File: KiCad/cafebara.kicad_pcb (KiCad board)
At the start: 4 copper layers, 49 x 32 mm, 54 parts, among them J1 Micro_SD_Card_Det2, J2 USB_C_Receptacle_USB2.0_14P, J3 PROG, J4 Conn_01x19_MountingPin, J5 I2C, J6 EDID, Q1 NMOS, SW1 SW_Push, U3 ATtiny1616-M, U4 M24C02-WMN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

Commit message: Various improvements and misc changes
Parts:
- added C17: 22uF, Capacitor_SMD:C_0402_1005Metric, F.Cu at (102.5, 68.0)
- added C18: 22uF, Capacitor_SMD:C_0402_1005Metric, F.Cu at (102.5, 67.0)
- added R9: 1k, Resistor_SMD:R_0402_1005Metric, F.Cu at (70.5, 52.0)
- C10, C11: value 10uF -> 22uF; footprint Capacitor_SMD:C_0402_1005Metric -> Capacitor_SMD:C_0805_2012Metric
- C7, J6: moved to F.Cu
- U4: value M24C02-WMN -> M24C02-RMC; footprint Package_SO:SOIC-8_3.9x4.9mm_P1.27mm -> cafebara:UFDFPN_RMC; moved to F.Cu
- moved TP3 17.5 mm to (113.8, 49.0)
- moved C7 17.0 mm to (70.0, 49.2), turned to 90 degrees
- moved TP2 15.5 mm to (90.5, 72.2), turned to 180 degrees
- moved J6 14.9 mm to (68.0, 52.5), turned to 0 degrees
- moved U4 13.9 mm to (67.8, 49.0)
- moved TP1 13.7 mm to (92.5, 72.2), turned to 180 degrees
- moved R4 13.6 mm to (111.5, 50.2), turned to -90 degrees
- moved TP10 13.2 mm to (113.8, 47.2), turned to 180 degrees
- moved TP6 11.2 mm to (87.5, 72.0), turned to 180 degrees
- moved C13 4.32 mm to (108.5, 71.5), turned to -45 degrees
- moved C15 3.18 mm to (94.8, 65.8), turned to 90 degrees
- moved J3 2.55 mm to (114.0, 51.8)
- moved C4 2.02 mm to (90.2, 58.8), turned to 180 degrees
- moved C11 1.90 mm to (106.5, 65.8)
- moved C9 1.75 mm to (92.8, 68.0)
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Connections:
- U3 pad 18: unconnected-(U3-PC3-Pad18) -> EN
- U3 pad 20: unconnected-(U3-PA1-Pad20) -> /LED
- U3 pad 6: /LED -> unconnected-(U3-PA5-Pad6)
- U3 pad 9: EN -> unconnected-(U3-PB5-Pad9)
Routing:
- net +5V: track 12.0 -> 36.3 mm, vias 2 -> 3
- net /HDMI_SDA: track 5.09 -> 23.8 mm, vias 1 -> 2
- net D-: track 2.12 -> 20.4 mm, vias 0 -> 1
- net D+: track 2.12 -> 19.7 mm, vias 0 -> 1
- net /HDMI_SCL: track 8.10 -> 23.9 mm, vias 1 -> 2
- net HPD: track 62.4 -> 72.9 mm
- net /LED: track 3.23 -> 9.06 mm
- net ~{INT}: track 27.2 -> 33.0 mm
- net SDA: track 46.3 -> 48.9 mm
- net SCL: track 38.1 -> 40.7 mm
- net /PA0: track 4.44 -> 6.86 mm
- net /EEPROM_~{WC}: track 2.08 -> 4.20 mm
- net EN: track 11.0 -> 9.24 mm, vias 0 -> 2
- net VBUS: vias 27 -> 21
- net GND: vias 49 -> 41
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- removed copper zone on In2.Cu, net +3.3V

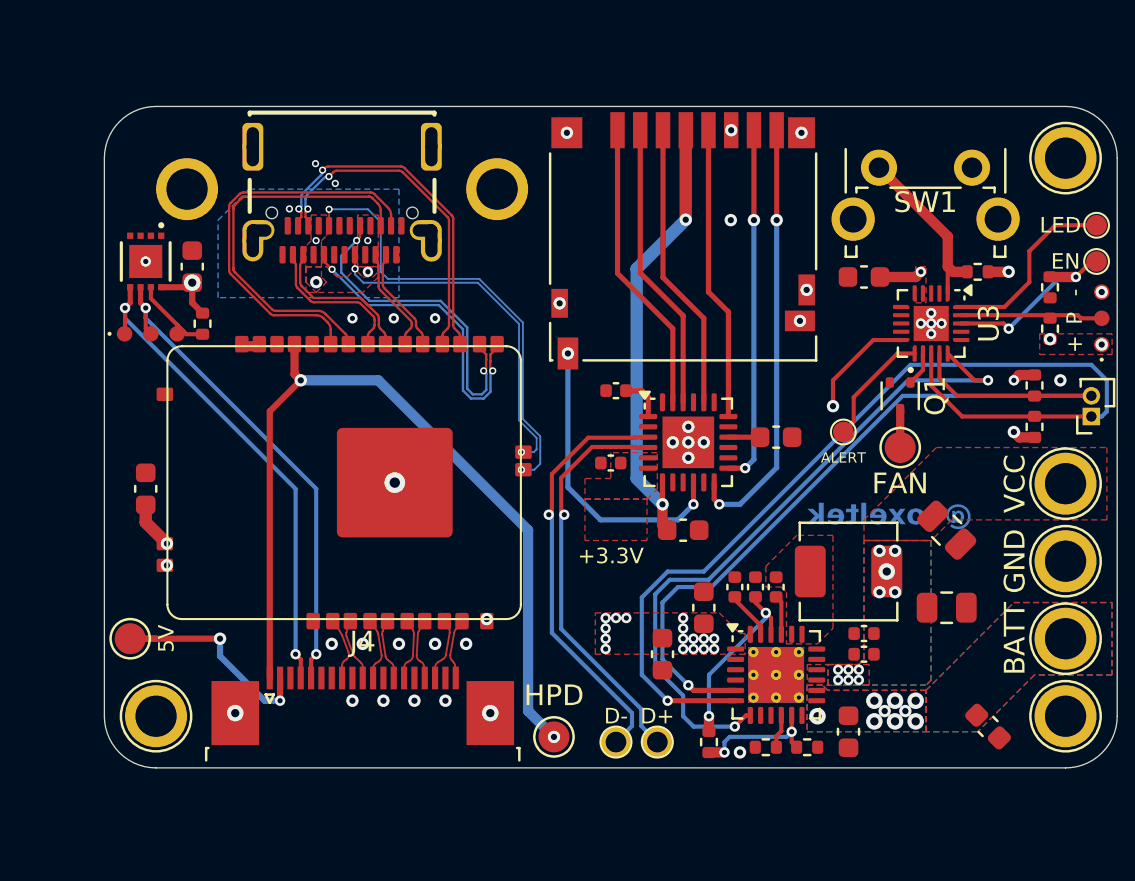
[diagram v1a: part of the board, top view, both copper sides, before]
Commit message: Misc improvements, 3D model generation
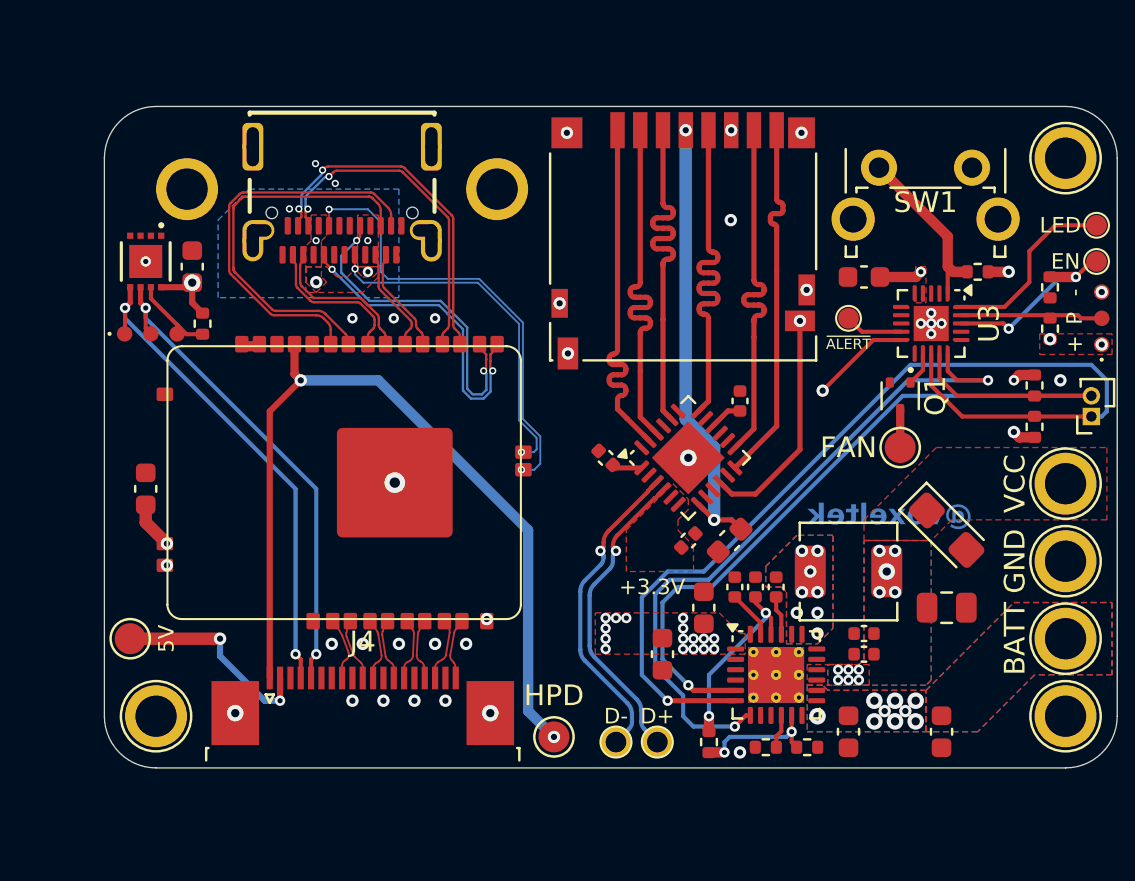
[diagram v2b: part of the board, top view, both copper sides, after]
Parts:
- removed C10: 22uF, Capacitor_SMD:C_0805_2012Metric
- added C19: 100uF, Capacitor_Tantalum_SMD:CP_EIA-3216-10_Kemet-I, F.Cu at (106.5, 62.0)
- C6: footprint Capacitor_SMD:C_0603_1608Metric -> Capacitor_SMD:C_0402_1005Metric
- TP7: value ALERT -> ~{ALERT}
- moved TP7 5.51 mm to (101.8, 51.8)
- moved C4 5.30 mm to (94.0, 62.5), turned to 45 degrees
- moved C3 3.29 mm to (90.0, 58.5), turned to 135 degrees
- moved C6 2.47 mm to (96.5, 55.8), turned to 90 degrees
- moved C5 2.30 mm to (96.0, 62.5), turned to -135 degrees
- moved C13 2.26 mm to (106.2, 71.8), turned to -90 degrees
- moved U2 0.75 mm to (94.0, 58.5), turned to 45 degrees
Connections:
- J1 pad 10: SD_DECT -> GND
- J1 pad 9: GND -> SD_DECT
- U3 pad 11: ~{ALERT} -> unconnected-(U3-PB3-Pad11)
- U3 pad 9: unconnected-(U3-PB5-Pad9) -> ~{ALERT}
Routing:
- net D-: track 20.4 -> 15.4 mm
- net D+: track 19.7 -> 15.0 mm
- net SD_CMD: track 14.0 -> 17.9 mm
- net SD_D3: track 14.0 -> 17.9 mm
- net SD_D2: track 14.3 -> 17.9 mm
- net SD_CLK: track 14.2 -> 17.9 mm
- net SD_DECT: track 14.6 -> 11.2 mm, vias 2 -> 1
- net SD_D1: track 21.0 -> 18.0 mm, vias 2 -> 0
- net ~{ALERT}: track 5.72 -> 2.82 mm
- net HPD: track 72.9 -> 72.2 mm
- net Net-(U2-VDD): track 2.15 -> 1.47 mm
- net SD_D0: track 17.3 -> 17.9 mm, vias 2 -> 0
- net Net-(C12-Pad1): vias 0 -> 8
- net GND: vias 41 -> 37
- added copper zone on B.Cu, net Net-(C12-Pad1)
- added copper zone on In2.Cu, net Net-(C12-Pad1)

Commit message: Several improvements
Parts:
- added C10: 10uF, Capacitor_SMD:C_0603_1608Metric, F.Cu at (91.2, 68.0)
- TP7: value ~{ALERT} -> ALERT
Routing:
- net Net-(C12-Pad1): vias 8 -> 0
- removed copper zone on B.Cu, net Net-(C12-Pad1)
- removed copper zone on In2.Cu, net Net-(C12-Pad1)

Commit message: Misc improvements to several boards
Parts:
- added C20: 10uF, Capacitor_SMD:C_0603_1608Metric, F.Cu at (107.8, 71.8)
- moved SW1 2.41 mm to (105.5, 45.2)
- moved C11 2.02 mm to (105.5, 67.5)
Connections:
- net ~{INT} renamed ~{BQ_INT}
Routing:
- net VCC: vias 17 -> 18
- net VBUS: vias 21 -> 20
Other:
- board text added: "SCL"
- board text added: "SDA"

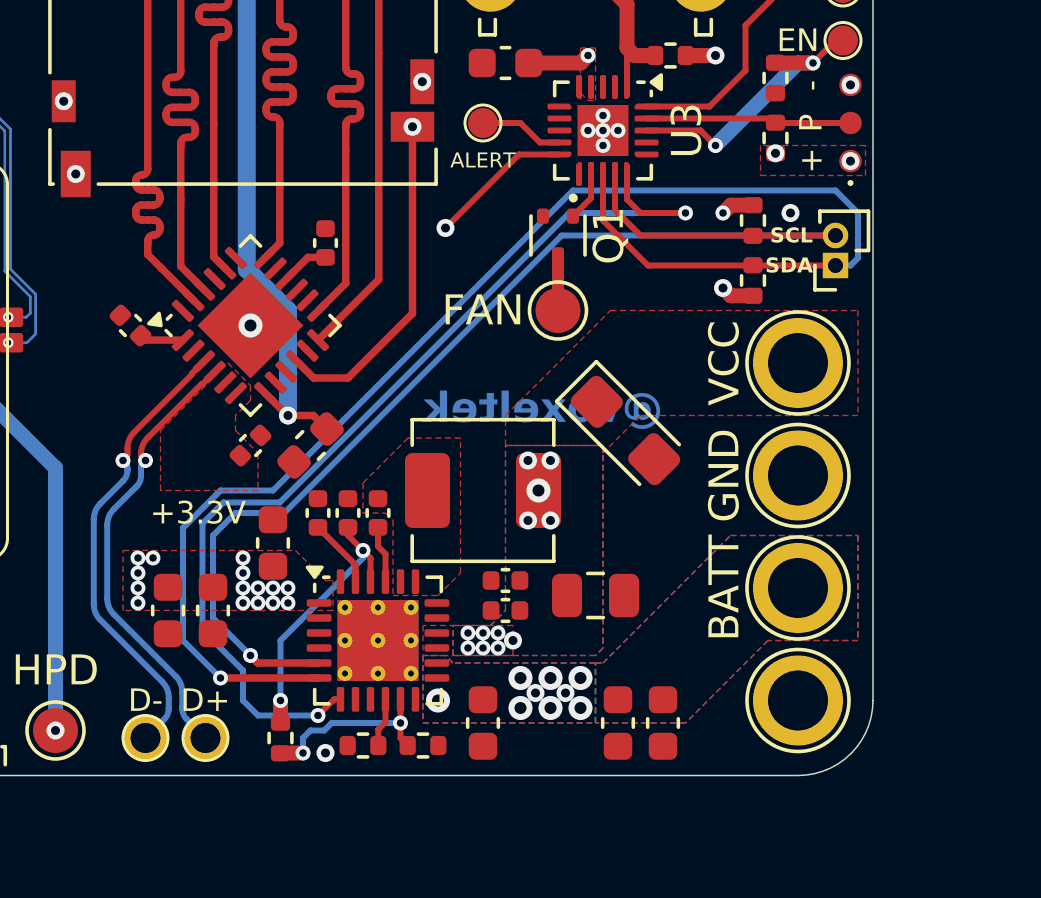
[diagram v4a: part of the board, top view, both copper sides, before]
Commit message: Misc improvements, firmware rewrite
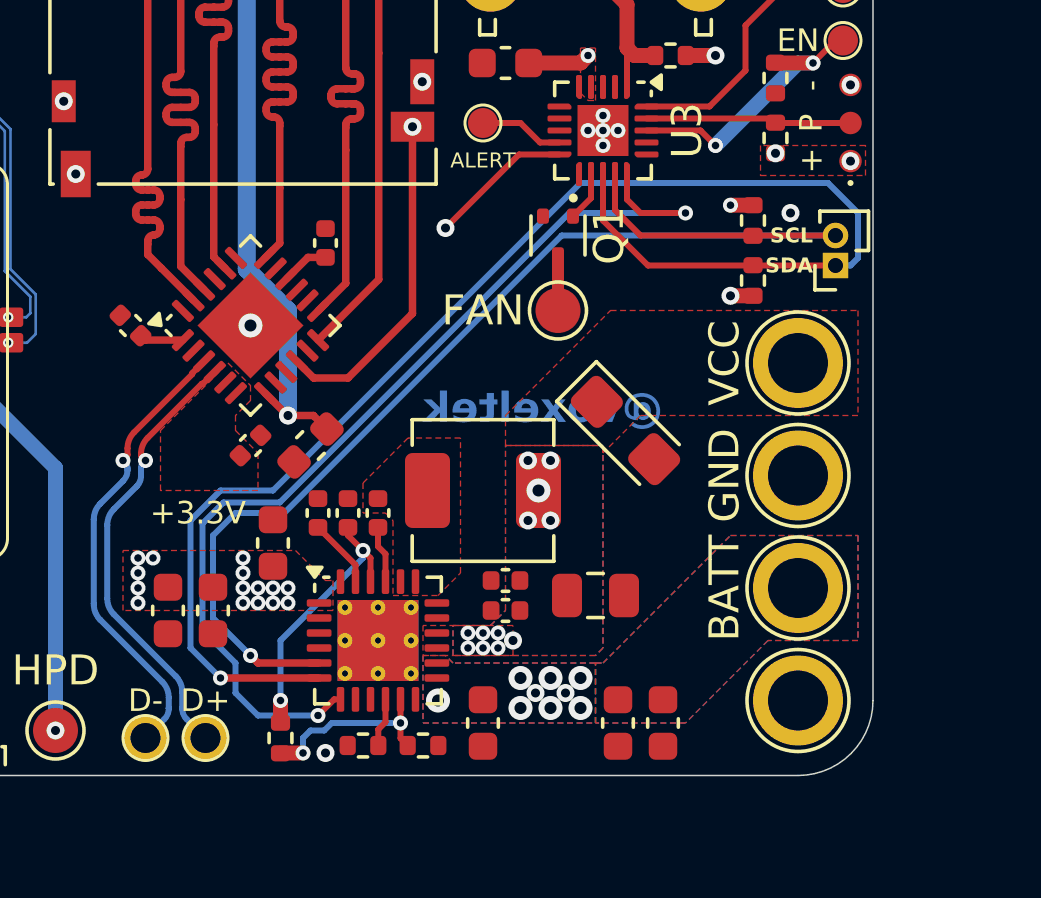
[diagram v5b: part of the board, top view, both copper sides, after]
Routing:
- net VCC: track 5.28 -> 4.57 mm

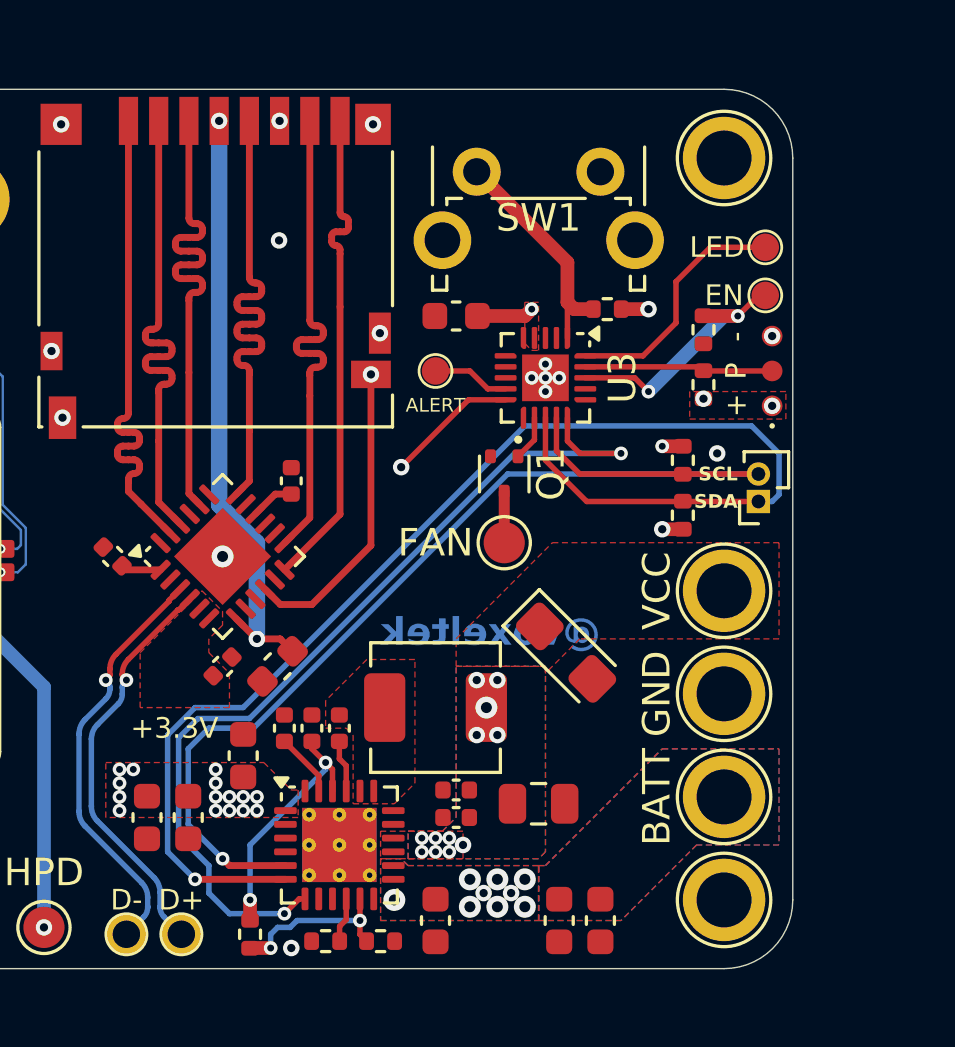
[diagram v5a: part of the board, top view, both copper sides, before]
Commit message: Rework, adding UART for Pi communication
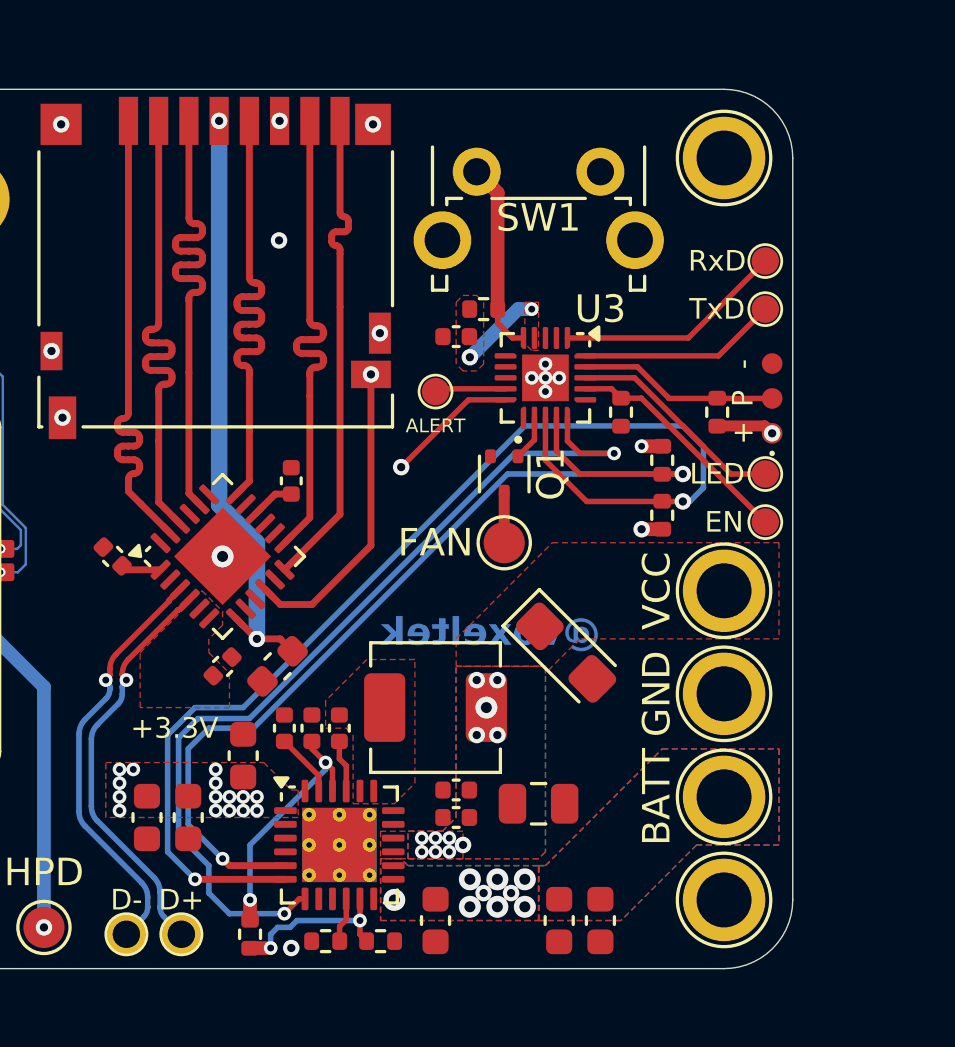
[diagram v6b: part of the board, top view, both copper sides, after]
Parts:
- removed J5: I2C, Connector_PinSocket_1.00mm:PinSocket_1x02_P1.00mm_Vertical
- added TP13: TxD, cafebara:TestPoint_Pad_D1.0mm_Small, F.Cu at (113.8, 49.5)
- added TP14: RxD, cafebara:TestPoint_Pad_D1.0mm_Small, F.Cu at (113.8, 47.8)
- C2: value 0.1uF -> 10uF; footprint Capacitor_SMD:C_0603_1608Metric -> Capacitor_SMD:C_0402_1005Metric
- moved TP3 8.25 mm to (113.8, 57.2)
- moved TP10 8.25 mm to (113.8, 55.5)
- moved R5 4.50 mm to (103.5, 49.5), turned to 180 degrees
- moved R4 4.24 mm to (108.5, 53.2)
- moved R3 1.12 mm to (112.0, 53.2)
- moved J3 1.00 mm to (114.0, 52.8)
- moved C2 0.75 mm to (102.5, 50.5)
- moved R1 0.75 mm to (110.0, 55.0)
- moved R2 0.75 mm to (110.0, 57.0)
- moved TP7 0.75 mm to (101.8, 52.5)
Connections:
- U3 pad 1: /PowerButton -> RxD
- U3 pad 17: unconnected-(U3-PC2-Pad17) -> EN
- U3 pad 18: EN -> /LED
- U3 pad 20: /LED -> TxD
- U3 pad 5: unconnected-(U3-PA4-Pad5) -> /PowerButton
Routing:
- net RxD: track 0.00 -> 8.36 mm
- net TxD: track 0.00 -> 7.25 mm
- net SDA: track 48.9 -> 43.1 mm, vias 1 -> 2
- net SCL: track 40.7 -> 35.2 mm, vias 1 -> 2
- net VCC: track 4.57 -> 6.59 mm, vias 18 -> 17
- net /PowerButton: track 8.46 -> 6.99 mm
- net /LED: track 9.06 -> 8.00 mm
- net EN: track 9.45 -> 8.56 mm, vias 2 -> 0
- net GND: vias 37 -> 35
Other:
- board text removed: "SCL"
- board text removed: "SDA"
